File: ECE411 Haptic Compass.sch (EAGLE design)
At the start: 41 parts, among them IC1 SN74LVC1G14DBVR, Q1 PBHV8115TLHR, Q2 PBHV8115TLHR, Q3 PBHV8115TLHR, Q4 PBHV8115TLHR, U1 328P, Y1 ECS-160-8-30Q-VY-TR

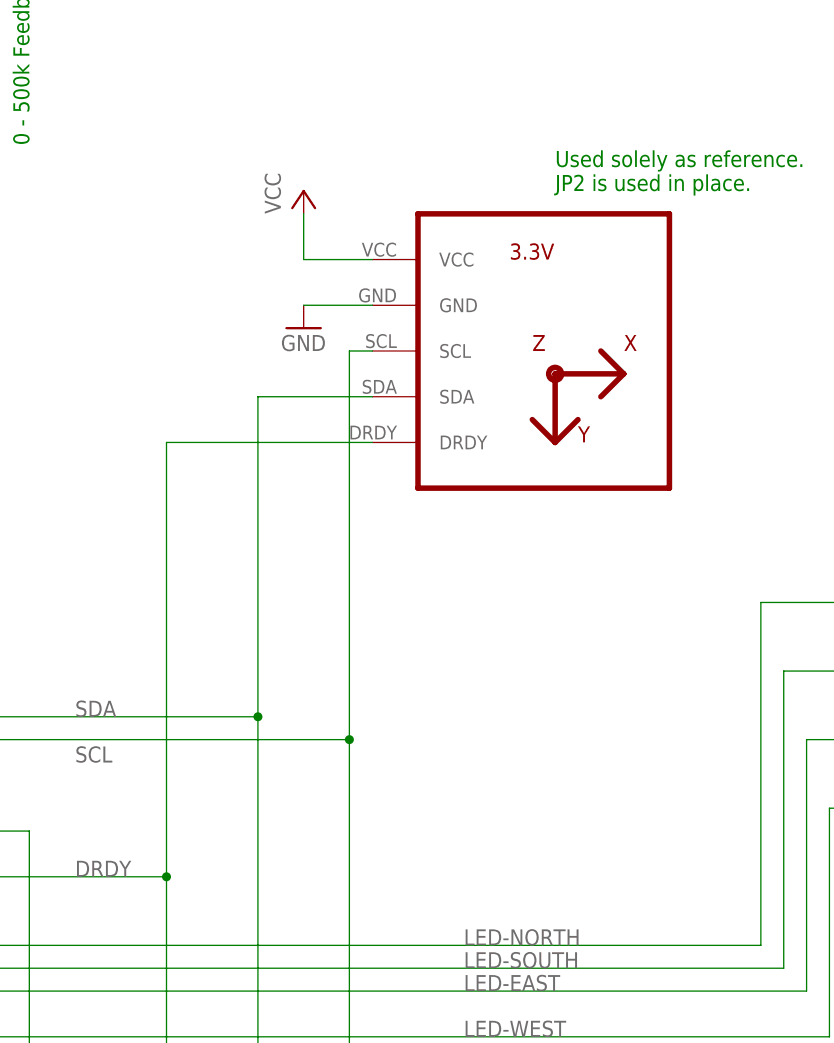
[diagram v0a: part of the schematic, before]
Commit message: Created Board Layout for Haptic Compass
Ground planes are left to be created. More will be done to it as revisions this week go through.
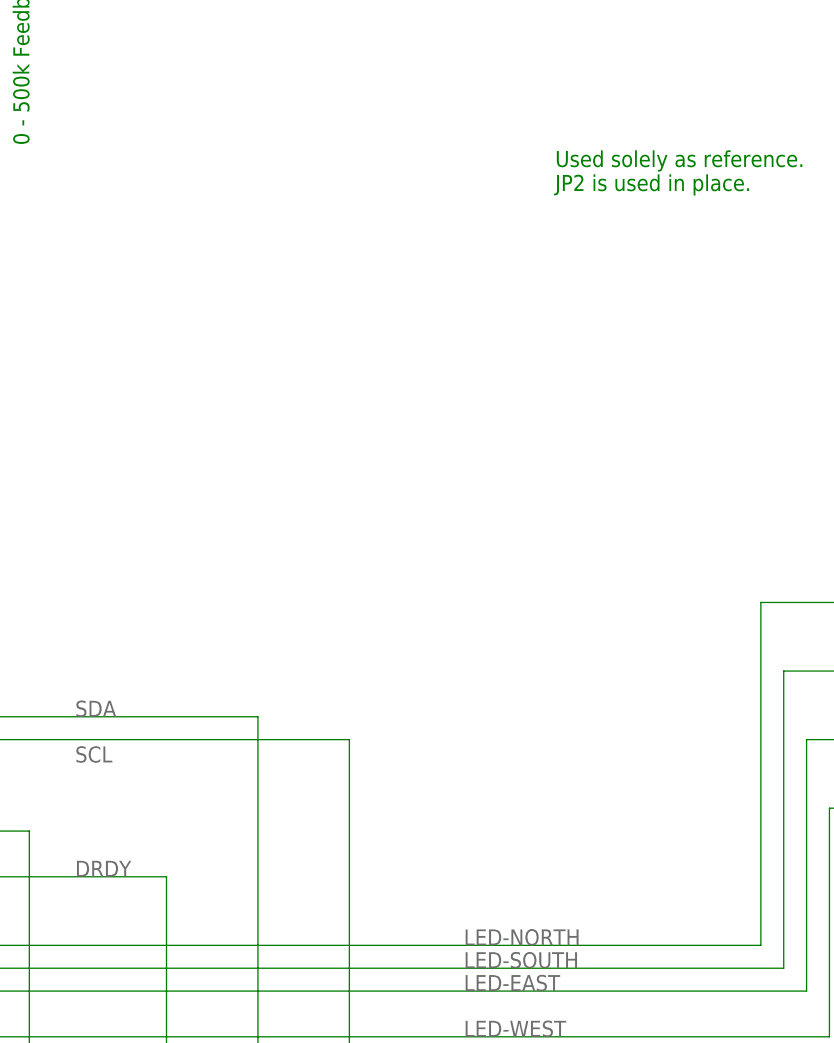
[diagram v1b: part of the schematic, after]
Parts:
- removed MAGNETOMETER: HMC5883LGY-271, hmc5883l:HMC5883LGY-271
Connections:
- net DRDY: no longer MAGNETOMETER.DRDY
- net GND: no longer MAGNETOMETER.GND
- net SCL: no longer MAGNETOMETER.SCL
- net SDA: no longer MAGNETOMETER.SDA
- net VCC: no longer MAGNETOMETER.VCC
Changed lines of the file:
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@@
 <groups>
 <schematic_group name="POWER-5V-REGULATED"/>
-<schematic_group name="MAGNETIC-SENSING"/>
 <schematic_group name="PROGRAMMING-IO"/>
 <schematic_group name="MAGNETOMETER-IO"/>
@@
 <parts>
 <part name="U1" library="SparkFun-IC-Microcontroller" library_urn="urn:adsk.eagle:library:525" deviceset="ATMEGA328P_PDIP" device="" package3d_urn="urn:adsk.eagle:package:38942/1" value="328P"/>
-<part name="MAGNETOMETER" library="hmc5883l" deviceset="HMC5883L" device="GY-271"/>
 <part name="R1" library="rcl" library_urn="urn:adsk.eagle:library:334" deviceset="R-US_" device="R0805" package3d_urn="urn:adsk.eagle:package:23553/2" value="100K"/>
 <part name="C1" library="rcl" library_urn="urn:adsk.eagle:library:334" deviceset="C-US" device="C0805" package3d_urn="urn:adsk.eagle:package:23617/2" value="220pF"/>
@@
 <part name="GND1" library="supply1" library_urn="urn:adsk.eagle:library:371" deviceset="GND" device=""/>
 <part name="GND2" library="supply1" library_urn="urn:adsk.eagle:library:371" deviceset="GND" device=""/>
-<part name="GND3" library="supply1" library_urn="urn:adsk.eagle:library:371" deviceset="GND" device=""/>
 <part name="P+2" library="supply1" library_urn="urn:adsk.eagle:library:371" deviceset="VCC" device=""/>
-<part name="P+3" library="supply1" library_urn="urn:adsk.eagle:library:371" deviceset="VCC" device=""/>
 <part name="C2" library="rcl" library_urn="urn:adsk.eagle:library:334" deviceset="C-US" device="C0805" package3d_urn="urn:adsk.eagle:package:23617/2" value="22pF"/>
 <part name="C3" library="rcl" library_urn="urn:adsk.eagle:library:334" deviceset="C-US" device="C0805" package3d_urn="urn:adsk.eagle:package:23617/2" value="22pF"/>
@@
 <attribute name="VALUE" x="43.18" y="7.62" size="1.778" layer="96"/>
 </instance>
-<instance part="MAGNETOMETER" gate="G$1" x="149.86" y="101.6" smashed="yes" grouprefs="MAGNETIC-SENSING"/>
 <instance part="R1" gate="G$1" x="30.48" y="144.78" smashed="yes" rot="R270" grouprefs="POWER-5V-REGULATED">
 <attribute name="NAME" x="26.67" y="146.2786" size="1.778" layer="95"/>
@@
 <attribute name="VALUE" x="15.24" y="20.32" size="1.778" layer="96"/>
 </instance>
-<instance part="GND3" gate="1" x="127" y="104.14" smashed="yes" grouprefs="MAGNETIC-SENSING">
-<attribute name="VALUE" x="124.46" y="101.6" size="1.778" layer="96"/>
-</instance>
 <instance part="P+2" gate="VCC" x="30.48" y="68.58" smashed="yes" grouprefs="PROCESSING">
 <attribute name="VALUE" x="27.94" y="68.58" size="1.778" layer="96" rot="R180"/>
-</instance>
-<instance part="P+3" gate="VCC" x="127" y="119.38" smashed="yes" grouprefs="MAGNETIC-SENSING">
-<attribute name="VALUE" x="124.46" y="116.84" size="1.778" layer="96" rot="R90"/>
 </instance>
 <instance part="C2" gate="G$1" x="33.02" y="35.56" smashed="yes" grouprefs="PROCESSING">
@@
 <pinref part="P+1" gate="VCC" pin="VCC"/>
 <junction x="71.12" y="177.8"/>
-</segment>
-<segment>
-<pinref part="MAGNETOMETER" gate="G$1" pin="VCC"/>
-<wire x1="134.62" y1="111.76" x2="127" y2="111.76" width="0.1524" layer="91" grouprefs="MAGNETIC-SENSING"/>
-<wire x1="127" y1="111.76" x2="127" y2="116.84" width="0.1524" layer="91" grouprefs="MAGNETIC-SENSING"/>
-<pinref part="P+3" gate="VCC" pin="VCC"/>
 </segment>
 <segment>
@@
 </segment>
 <segment>
-<pinref part="MAGNETOMETER" gate="G$1" pin="GND"/>
-<wire x1="134.62" y1="106.68" x2="127" y2="106.68" width="0.1524" layer="91" grouprefs="MAGNETIC-SENSING"/>
-<pinref part="GND3" gate="1" pin="GND"/>
-</segment>
-<segment>
 <pinref part="C2" gate="G$1" pin="2"/>
 <wire x1="33.02" y1="30.48" x2="33.02" y2="27.94" width="0.1524" layer="91" grouprefs="PROCESSING"/>
@@
 <net name="SDA" class="0">
 <segment>
-<pinref part="MAGNETOMETER" gate="G$1" pin="SDA"/>
-<wire x1="134.62" y1="96.52" x2="121.92" y2="96.52" width="0.1524" layer="91"/>
-<wire x1="121.92" y1="96.52" x2="121.92" y2="60.96" width="0.1524" layer="91"/>
 <pinref part="U1" gate="G$1" pin="PC4(ADC4/SDA)"/>
 <label x="101.6" y="60.96" size="1.778" layer="95"/>
 <wire x1="121.92" y1="60.96" x2="86.36" y2="60.96" width="0.1524" layer="91"/>
-<junction x="121.92" y="60.96"/>
 <wire x1="121.92" y1="-25.4" x2="121.92" y2="60.96" width="0.1524" layer="91"/>
 <pinref part="R5" gate="G$1" pin="1"/>
@@
 <net name="SCL" class="0">
 <segment>
-<pinref part="MAGNETOMETER" gate="G$1" pin="SCL"/>
-<wire x1="134.62" y1="101.6" x2="132.08" y2="101.6" width="0.1524" layer="91"/>
-<wire x1="132.08" y1="101.6" x2="132.08" y2="58.42" width="0.1524" layer="91"/>
 <pinref part="U1" gate="G$1" pin="PC5(ADC5/SCL)"/>
 <label x="101.6" y="55.88" size="1.778" layer="95"/>
 <wire x1="132.08" y1="58.42" x2="86.36" y2="58.42" width="0.1524" layer="91"/>
-<junction x="132.08" y="58.42"/>
 <wire x1="132.08" y1="-25.4" x2="132.08" y2="58.42" width="0.1524" layer="91"/>
 <pinref part="R6" gate="G$1" pin="1"/>
@@
 <pinref part="U1" gate="G$1" pin="PD2(INT0)"/>
 <wire x1="86.36" y1="43.18" x2="111.76" y2="43.18" width="0.1524" layer="91"/>
-<wire x1="111.76" y1="43.18" x2="111.76" y2="91.44" width="0.1524" layer="91"/>
-<pinref part="MAGNETOMETER" gate="G$1" pin="DRDY"/>
-<wire x1="111.76" y1="91.44" x2="134.62" y2="91.44" width="0.1524" layer="91"/>
 <label x="101.6" y="43.18" size="1.778" layer="95"/>
-<junction x="111.76" y="43.18"/>
 <wire x1="111.76" y1="-25.4" x2="111.76" y2="43.18" width="0.1524" layer="91"/>
 <pinref part="R4" gate="G$1" pin="1"/>

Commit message: Included 1uF Capacitor next to Vcc for the uPC
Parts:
- added C6: 1uF, rcl:C-USC0805
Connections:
- net GND: now also C6.2
- net VCC: now also C6.1
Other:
- note removed: "Used solely as reference. JP2 is used in place."
- moved on the sheet: 3.7V-LIPO-1, 3.7V-LIPO-2, C1, Q1, Q2, Q3, Q4, R1, R2, R3, SPST-SLIDE-SWITCH, VR1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

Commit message: Board Final
Added AVCC, AGND, and VCC bypass capacitors and connected AGND and GND.
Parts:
- added C7, C8, C9: 0.1uF, rcl:C-USC0805
- C1: value 220pF -> 2220pF
- C6: value 1uF -> 0.1uF
- R13: value 1500 -> 1.5K
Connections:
- new net VREF: C8.1, U1.AREF
- net GND: now also C7.2, C8.2, C9.2, U1.GND@2
- net VCC: now also C7.1, C9.1, U1.AVCC
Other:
- moved on the sheet: 3.7V-LIPO-1, 3.7V-LIPO-2, C1, C2, C3, C4, C5, C6, D2, IC1, JP4, Q1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
